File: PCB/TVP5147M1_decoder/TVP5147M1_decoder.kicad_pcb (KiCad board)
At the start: 4 copper layers, 77 parts, among them J1 Conn_02x05_Odd_Even, J2 Conn_02x05_Odd_Even, J3 Conn_02x05_Odd_Even, J4 Conn_02x01, J5 Conn_01x03_Pin, U1 AMS1117-1.8, U2 TVP5147M1IPFP, Y1 14.31818 MHz

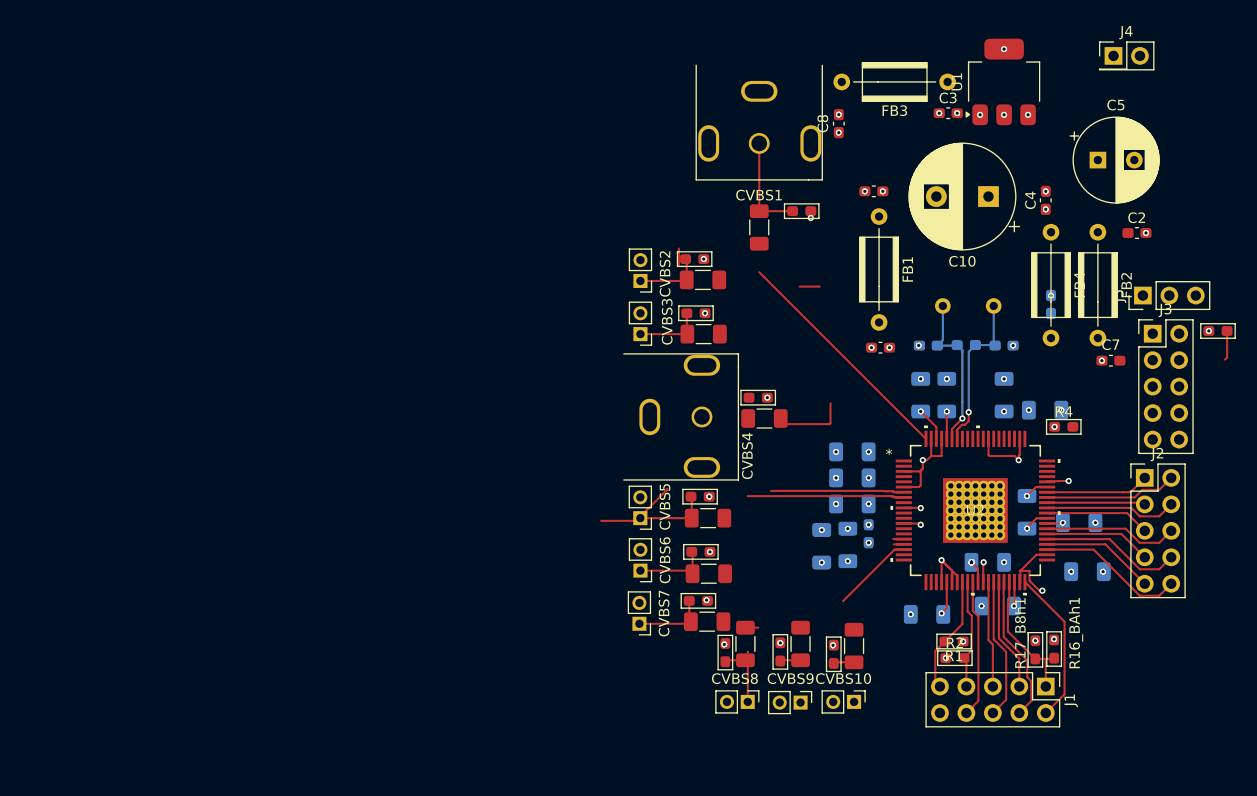
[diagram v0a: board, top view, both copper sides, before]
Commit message: decoder pcb almost done
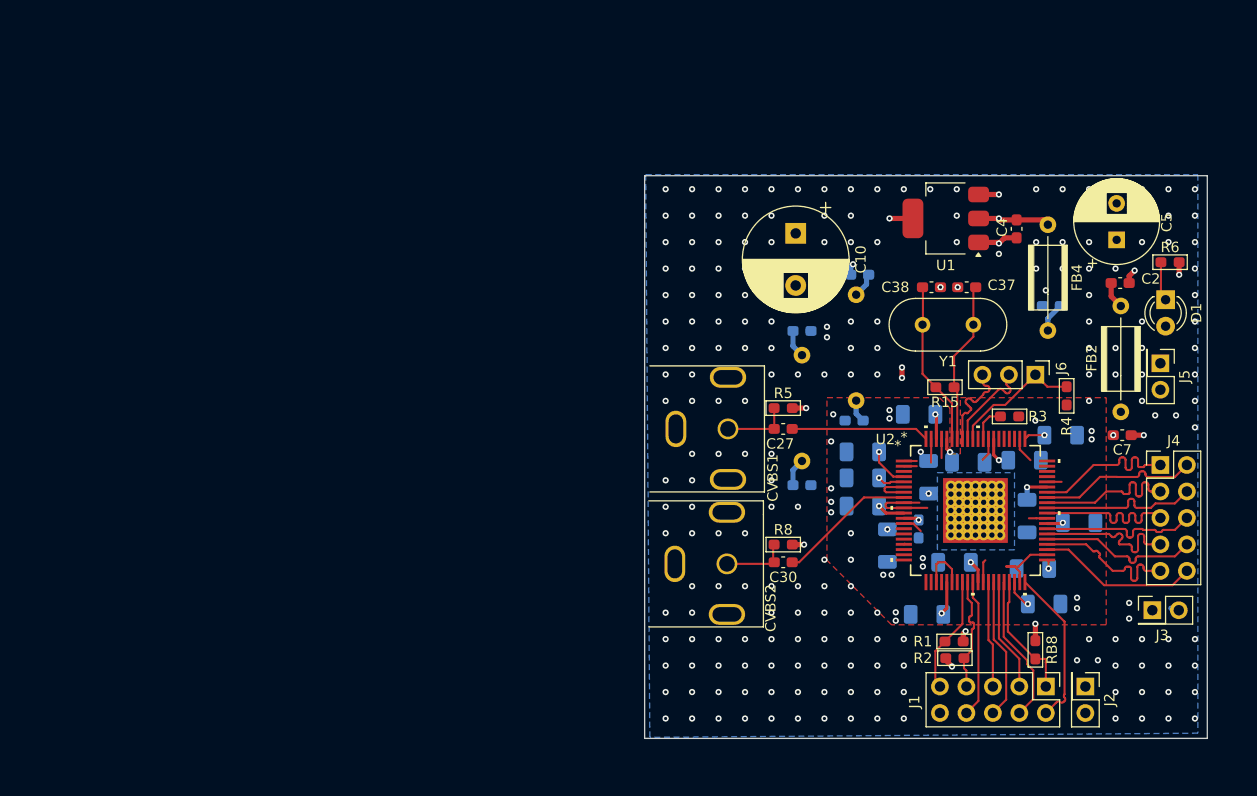
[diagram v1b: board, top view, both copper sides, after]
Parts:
- removed C28, C29, C31, C32, C33, C34, C35, C36: 0.1uF, Capacitor_SMD:C_1206_3216Metric_Pad1.33x1.80mm_HandSolder
- removed CVBS10, CVBS3, CVBS5, CVBS6, CVBS7, CVBS9: Conn_01x02, Connector_PinHeader_2.00mm:PinHeader_1x02_P2.00mm_Vertical
- removed the CVBS2 at (93.1, 69.6)
- removed CVBS8: Conn_Coaxial, Connector_PinHeader_2.00mm:PinHeader_1x02_P2.00mm_Vertical
- removed R10, R11, R12, R13, R14, R7, R9: 75Ohm, PCM_Resistor_SMD_AKL:R_0603_1608Metric_Pad1.05x0.95mm_HandSolder
- removed R16_BAh1: 10kOhm, PCM_Resistor_SMD_AKL:R_0603_1608Metric_Pad1.05x0.95mm_HandSolder
- added D1: LED_3mm, LED_THT:LED_D3.0mm, F.Cu at (143.5, 71.4)
- added J2: Conn_02x01, Connector_PinHeader_2.54mm:PinHeader_2x01_P2.54mm_Vertical, F.Cu at (135.8, 108.5)
- added NT1: NetTie_2, NetTie:NetTie-2_SMD_Pad0.5mm, F.Cu at (118.2, 78.4)
- C1, C3, C6, C8, FB1, FB3: moved to B.Cu
- C27, C30: footprint Capacitor_SMD:C_1206_3216Metric_Pad1.33x1.80mm_HandSolder -> Capacitor_SMD:C_0603_1608Metric_Pad1.08x0.95mm_HandSolder
- C37, C38, R15, Y1: moved to F.Cu
- J3: value Conn_02x05_Odd_Even -> Conn_02x01; footprint Connector_PinHeader_2.54mm:PinHeader_2x05_P2.54mm_Vertical -> Connector_PinHeader_2.54mm:PinHeader_2x01_P2.54mm_Vertical
- R6: value 75Ohm -> 5k
- moved R6 45.6 mm to (143.9, 67.8)
- moved J5 29.8 mm to (143.0, 77.5), turned to -90 degrees
- moved C8 28.5 mm to (113.6, 83.0), turned to 180 degrees
- moved J3 26.5 mm to (142.2, 101.2)
- moved FB3 22.2 mm to (113.8, 70.9), turned to -90 degrees
- moved R3 21.6 mm to (128.5, 82.6), turned to 180 degrees
- moved CVBS1 20.6 mm to (109.0, 84.0), turned to 90 degrees
- moved C27 19.5 mm to (106.8, 83.8), turned to 180 degrees
- moved R5 19.0 mm to (106.8, 81.8)
- moved C10 18.8 mm to (108.0, 65.0), turned to -90 degrees
- moved C3 17.7 mm to (114.1, 69.0), turned to 180 degrees
- moved FB1 15.2 mm to (108.6, 76.7)
- moved C6 15.2 mm to (108.6, 89.2), turned to 0 degrees
- moved C1 15.1 mm to (108.6, 74.4), turned to 0 degrees
- moved CVBS2 14.3 mm to (108.9, 96.9)
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- renumbered CVBS4 to CVBS2, J2 to J4, J4 to J5, J5 to J6, R17_B8h1 to RB8
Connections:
- C30 pad 1: CVBS_VI_2_A -> CVBS_VI_2_B
- C37 pad 2: GND -> XGND
- C38 pad 2: GND -> XGND
- J1 pad 10: unconnected-(J1-Pin_10-Pad10) -> GND
- J3 pad 1: C0 -> GND
- J3 pad 2: C1 -> GND
- R3 pad 2: C1 -> /C1
- U2 pad 1: CVBS_VI_1_B -> GND
- U2 pad 16: CVBS_VI_3_A -> GND
- U2 pad 17: CVBS_VI_3_B -> GND
- U2 pad 18: CVBS_VI_3_C -> GND
- U2 pad 2: CVBS_VI_1_C -> GND
- U2 pad 23: CVBS_VI_4_A -> GND
- U2 pad 57: C9 -> unconnected-(U2-C_9/GPIO9-Pad57)
- U2 pad 58: C8 -> unconnected-(U2-C_8/GPIO8-Pad58)
- U2 pad 59: C7 -> unconnected-(U2-C_7/GPIO7-Pad59)
- U2 pad 60: C6 -> unconnected-(U2-C_6/GPIO6-Pad60)
- U2 pad 63: C5 -> unconnected-(U2-C_5/GPIO5-Pad63)
- U2 pad 64: C4 -> unconnected-(U2-C_4/GPIO4-Pad64)
- U2 pad 65: C3 -> unconnected-(U2-C_3/GPIO3-Pad65)
- U2 pad 66: C2 -> unconnected-(U2-C_2/GPIO2-Pad66)
- U2 pad 69: C1 -> /C1
- U2 pad 7: CVBS_VI_2_A -> GND
- U2 pad 70: C0 -> unconnected-(U2-C_0/GPIO0-Pad70)
- U2 pad 9: CVBS_VI_2_C -> GND
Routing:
- net CVBS_VI_2_A: track 19.2 -> 0.00 mm
- net Net-(CVBS5-Pin_1): track 14.8 -> 0.00 mm
- net FID: track 0.00 -> 12.8 mm
- net GND: track 43.1 -> 54.1 mm, vias 48 -> 231
- net +1.8V: track 0.00 -> 11.1 mm, vias 4 -> 2
- net CVBS_VI_1_A: track 24.3 -> 13.2 mm
- net A3.3VDD: track 0.00 -> 9.27 mm, vias 3 -> 2
- net HS/CS: track 0.00 -> 9.26 mm
- net VS/VBLK: track 0.00 -> 9.25 mm
- net CVBS_VI_3_C: track 7.89 -> 0.00 mm
- net D1.8VDD: track 4.44 -> 12.3 mm, vias 7 -> 4
- net Net-(CVBS7-Pin_1): track 7.36 -> 0.00 mm
- net Net-(CVBS6-Pin_1): track 7.26 -> 0.00 mm
- net +3.3V: track 0.00 -> 7.21 mm, vias 2 -> 1
- net Net-(CVBS8-Pin_1): track 7.11 -> 0.00 mm
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- added copper zone on B.Cu, net GND
- added copper zone on F.Cu, net GND
- added copper zone on In1.Cu, net XGND
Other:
- board outline added: 54 x 54 mm

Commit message: added basic hash_drbg
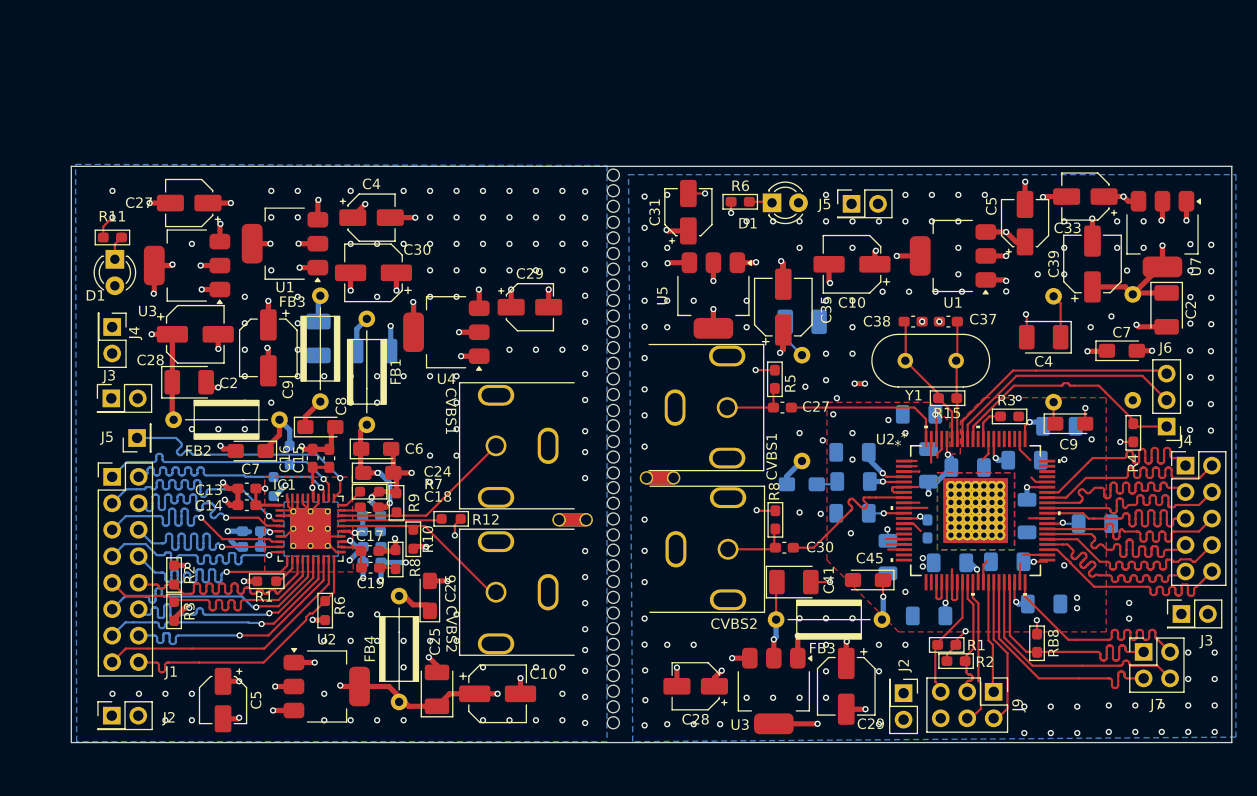
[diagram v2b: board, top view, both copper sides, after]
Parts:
- removed the FB3 at (113.8, 70.9)
- added C1: 33uF, Capacitor_Tantalum_SMD:CP_EIA-3528-15_AVX-H_Pad1.50x2.35mm_HandSolder, B.Cu at (67.4, 76.3)
- added C10: 22uF, Capacitor_SMD:CP_Elec_5x5.7, F.Cu at (79.4, 109.2)
- added C11: 0.01uF, Capacitor_SMD:C_0603_1608Metric_Pad1.08x0.95mm_HandSolder, B.Cu at (55.8, 95.1)
- added C12: 0.1uF, Capacitor_SMD:C_0603_1608Metric_Pad1.08x0.95mm_HandSolder, B.Cu at (55.8, 93.6)
- added C13: 0.01uF, Capacitor_SMD:C_0603_1608Metric_Pad1.08x0.95mm_HandSolder, F.Cu at (55.3, 89.5)
- added C14: 0.1uF, Capacitor_SMD:C_0603_1608Metric_Pad1.08x0.95mm_HandSolder, F.Cu at (55.3, 91.1)
- added C15: 0.01uF, Capacitor_SMD:C_0603_1608Metric_Pad1.08x0.95mm_HandSolder, F.Cu at (63.2, 86.6)
- added C16: 0.1uF, Capacitor_SMD:C_0603_1608Metric_Pad1.08x0.95mm_HandSolder, F.Cu at (61.6, 86.6)
- added C17: 12nF, Capacitor_SMD:C_0603_1608Metric_Pad1.08x0.95mm_HandSolder, F.Cu at (67.1, 95.5)
- added C18: 2.2nF, Capacitor_SMD:C_0603_1608Metric_Pad1.08x0.95mm_HandSolder, F.Cu at (67.1, 91.3)
- added C19: 150nF, Capacitor_SMD:C_0603_1608Metric_Pad1.08x0.95mm_HandSolder, F.Cu at (67.2, 97.1)
- added C2: 33uF, Capacitor_Tantalum_SMD:CP_EIA-3528-15_AVX-H_Pad1.50x2.35mm_HandSolder, F.Cu at (49.8, 79.3)
- added C20: 0.01uF, Capacitor_SMD:C_0603_1608Metric_Pad1.08x0.95mm_HandSolder, B.Cu at (67.3, 95.1)
- added C21: 0.1uF, Capacitor_SMD:C_0603_1608Metric_Pad1.08x0.95mm_HandSolder, B.Cu at (67.3, 96.6)
- added C22: 0.01uF, Capacitor_SMD:C_0603_1608Metric_Pad1.08x0.95mm_HandSolder, B.Cu at (67.3, 92.1)
- added C23: 0.1uF, Capacitor_SMD:C_0603_1608Metric_Pad1.08x0.95mm_HandSolder, B.Cu at (67.3, 93.6)
- added C24: 1uF, Capacitor_Tantalum_SMD:CP_EIA-3216-18_Kemet-A_Pad1.58x1.35mm_HandSolder, F.Cu at (67.9, 88.0)
- added C25: 33uF, Capacitor_Tantalum_SMD:CP_EIA-3528-15_AVX-H_Pad1.50x2.35mm_HandSolder, F.Cu at (73.6, 108.8)
- added C26: 10uF, Capacitor_Tantalum_SMD:CP_EIA-3216-18_Kemet-A_Pad1.58x1.35mm_HandSolder, F.Cu at (72.9, 99.8)
- added C27: 10uF, Capacitor_SMD:CP_Elec_4x5.7, F.Cu at (49.8, 62.1)
- added C28: 22uF, Capacitor_SMD:CP_Elec_5x5.7, F.Cu at (50.4, 74.7)
- added C28: 10uF, Capacitor_SMD:CP_Elec_4x5.7, F.Cu at (98.4, 108.5)
- added C29: 10uF, Capacitor_SMD:CP_Elec_4x5.7, F.Cu at (82.5, 72.1)
- added C29: 22uF, Capacitor_SMD:CP_Elec_5x5.7, F.Cu at (112.8, 108.5)
- added C30: 22uF, Capacitor_SMD:CP_Elec_5x5.7, F.Cu at (67.5, 68.8)
- added C31: 10uF, Capacitor_SMD:CP_Elec_4x5.7, F.Cu at (97.7, 63.0)
- added C33: 10uF, Capacitor_SMD:CP_Elec_4x5.7, F.Cu at (135.8, 61.5)
- added C35: 22uF, Capacitor_SMD:CP_Elec_5x5.7, F.Cu at (106.8, 72.1)
- added C39: 22uF, Capacitor_SMD:CP_Elec_5x5.7, F.Cu at (136.5, 68.0)
- added C4: 10uF, Capacitor_SMD:CP_Elec_4x5.7, F.Cu at (67.3, 63.5)
- added C41: 33uF, Capacitor_Tantalum_SMD:CP_EIA-3528-15_AVX-H_Pad1.50x2.35mm_HandSolder, F.Cu at (107.8, 98.5)
- added C45: 10uF, Capacitor_Tantalum_SMD:CP_EIA-3216-18_Kemet-A_Pad1.58x1.35mm_HandSolder, F.Cu at (114.9, 98.3)
- added C5: 10uF, Capacitor_SMD:CP_Elec_4x5.7, F.Cu at (53.0, 109.8)
- added C6: 10uF, Capacitor_Tantalum_SMD:CP_EIA-3216-18_Kemet-A_Pad1.58x1.35mm_HandSolder, F.Cu at (67.7, 85.7)
- added C7: 10uF, Capacitor_Tantalum_SMD:CP_EIA-3216-18_Kemet-A_Pad1.58x1.35mm_HandSolder, F.Cu at (55.7, 85.9)
- added C9: 22uF, Capacitor_SMD:CP_Elec_5x5.7, F.Cu at (57.4, 76.0)
- added CVBS1: Conn_Coaxial, LocalLibrary:CC-132-B1, F.Cu at (71.7, 85.3)
- added CVBS2: Conn_Coaxial, LocalLibrary:CC-132-B1, F.Cu at (71.7, 99.3)
- added D1: LED_3mm, LED_THT:LED_D3.0mm, F.Cu at (42.7, 67.5)
- added FB1: Ferrite_Bead, PCM_Ferrite_THT_AKL:Ferrite_L6.0mm_D3.5mm_P10.16mm, F.Cu at (66.8, 73.2)
- added FB2: Ferrite_Bead, PCM_Ferrite_THT_AKL:Ferrite_L6.0mm_D3.5mm_P10.16mm, F.Cu at (48.3, 82.9)
- added FB3: Ferrite_Bead, PCM_Ferrite_THT_AKL:Ferrite_L6.0mm_D3.5mm_P10.16mm, F.Cu at (106.1, 102.1)
- added FB3: Ferrite_Bead, PCM_Ferrite_THT_AKL:Ferrite_L6.0mm_D3.5mm_P10.16mm, F.Cu at (62.4, 71.0)
- added FB4: Ferrite_Bead, PCM_Ferrite_THT_AKL:Ferrite_L6.0mm_D3.5mm_P10.16mm, F.Cu at (69.9, 110.0)
- added IC1: ADV7393BCPZ-REEL, Package_CSP:LFCSP-40-1EP_6x6mm_P0.5mm_EP3.9x3.9mm_ThermalVias, F.Cu at (61.4, 93.4)
- added J2: Conn_02x01, Connector_PinHeader_2.54mm:PinHeader_2x01_P2.54mm_Vertical, F.Cu at (42.4, 111.3)
- added J3: Conn_02x01, Connector_PinHeader_2.54mm:PinHeader_2x01_P2.54mm_Vertical, F.Cu at (42.3, 80.9)
- added J4: Conn_02x01, Connector_PinHeader_2.54mm:PinHeader_2x01_P2.54mm_Vertical, F.Cu at (42.4, 74.0)
- added J5: Conn_01x01, Connector_PinHeader_2.54mm:PinHeader_1x01_P2.54mm_Vertical, F.Cu at (44.8, 84.7)
- added J7: Conn_02x02_Odd_Even, Connector_PinHeader_2.54mm:PinHeader_2x02_P2.54mm_Vertical, F.Cu at (141.4, 105.2)
- added J9: Conn_02x03_Odd_Even, Connector_PinHeader_2.54mm:PinHeader_2x03_P2.54mm_Vertical, F.Cu at (127.0, 109.0)
- added NT1: NetTie_2, NetTie:NetTie-2_THT_Pad1.0mm, F.Cu at (87.9, 92.5)
- added NT3: NetTie_2, NetTie:NetTie-2_THT_Pad1.0mm, F.Cu at (96.3, 88.5)
- added R1: 5k, PCM_Resistor_SMD_AKL:R_0603_1608Metric_Pad0.98x0.95mm_HandSolder, F.Cu at (57.2, 98.4)
- added R10: 75, PCM_Resistor_SMD_AKL:R_0603_1608Metric_Pad0.98x0.95mm_HandSolder, F.Cu at (71.3, 94.4)
- added R11: 5k, PCM_Resistor_SMD_AKL:R_0603_1608Metric_Pad1.05x0.95mm_HandSolder, F.Cu at (42.4, 65.4)
- added R12: 0, PCM_Resistor_SMD_AKL:R_0603_1608Metric_Pad0.98x0.95mm_HandSolder, F.Cu at (74.9, 92.4)
- added R2: 2k2, PCM_Resistor_SMD_AKL:R_0603_1608Metric_Pad0.98x0.95mm_HandSolder, F.Cu at (48.3, 97.8)
- added R3: 2k2, PCM_Resistor_SMD_AKL:R_0603_1608Metric_Pad0.98x0.95mm_HandSolder, F.Cu at (48.3, 101.3)
- added R4: 4k7, PCM_Resistor_SMD_AKL:R_0603_1608Metric_Pad0.98x0.95mm_HandSolder, B.Cu at (57.9, 89.3)
- added R5: 4k7, PCM_Resistor_SMD_AKL:R_0603_1608Metric_Pad0.98x0.95mm_HandSolder, B.Cu at (59.4, 86.3)
- added R6: 4k7, PCM_Resistor_SMD_AKL:R_0603_1608Metric_Pad0.98x0.95mm_HandSolder, F.Cu at (62.8, 101.2)
- added R7: 510, PCM_Resistor_SMD_AKL:R_0603_1608Metric_Pad0.98x0.95mm_HandSolder, F.Cu at (67.1, 89.8)
- added R8: 170, PCM_Resistor_SMD_AKL:R_0603_1608Metric_Pad0.98x0.95mm_HandSolder, F.Cu at (69.6, 96.3)
- added R9: 75, PCM_Resistor_SMD_AKL:R_0603_1608Metric_Pad0.98x0.95mm_HandSolder, F.Cu at (69.7, 90.9)
- added REF**: ToolingHole_1.152mm, MountingHole:ToolingHole_1.152mm, F.Cu at (90.5, 110.5)
- added REF**: ToolingHole_1.152mm, MountingHole:ToolingHole_1.152mm, F.Cu at (90.5, 109.0)
- added REF**: ToolingHole_1.152mm, MountingHole:ToolingHole_1.152mm, F.Cu at (90.5, 89.4)
- added REF**: ToolingHole_1.152mm, MountingHole:ToolingHole_1.152mm, F.Cu at (90.5, 68.5)
- added REF**: ToolingHole_1.152mm, MountingHole:ToolingHole_1.152mm, F.Cu at (90.5, 83.5)
- added REF**: ToolingHole_1.152mm, MountingHole:ToolingHole_1.152mm, F.Cu at (90.5, 90.9)
- added REF**: ToolingHole_1.152mm, MountingHole:ToolingHole_1.152mm, F.Cu at (90.5, 96.9)
- added REF**: ToolingHole_1.152mm, MountingHole:ToolingHole_1.152mm, F.Cu at (90.5, 107.5)
- added REF**: ToolingHole_1.152mm, MountingHole:ToolingHole_1.152mm, F.Cu at (90.5, 77.5)
- added REF**: ToolingHole_1.152mm, MountingHole:ToolingHole_1.152mm, F.Cu at (90.5, 67.0)
- added REF**: ToolingHole_1.152mm, MountingHole:ToolingHole_1.152mm, F.Cu at (90.5, 104.5)
- added REF**: ToolingHole_1.152mm, MountingHole:ToolingHole_1.152mm, F.Cu at (90.5, 88.0)
- added REF**: ToolingHole_1.152mm, MountingHole:ToolingHole_1.152mm, F.Cu at (90.5, 62.4)
- added REF**: ToolingHole_1.152mm, MountingHole:ToolingHole_1.152mm, F.Cu at (90.5, 106.0)
- added REF**: ToolingHole_1.152mm, MountingHole:ToolingHole_1.152mm, F.Cu at (90.5, 112.0)
- added REF**: ToolingHole_1.152mm, MountingHole:ToolingHole_1.152mm, F.Cu at (90.5, 100.0)
- added REF**: ToolingHole_1.152mm, MountingHole:ToolingHole_1.152mm, F.Cu at (90.5, 74.5)
- added REF**: ToolingHole_1.152mm, MountingHole:ToolingHole_1.152mm, F.Cu at (90.5, 98.4)
- added REF**: ToolingHole_1.152mm, MountingHole:ToolingHole_1.152mm, F.Cu at (90.5, 60.9)
- added REF**: ToolingHole_1.152mm, MountingHole:ToolingHole_1.152mm, F.Cu at (90.5, 86.5)
- added REF**: ToolingHole_1.152mm, MountingHole:ToolingHole_1.152mm, F.Cu at (90.5, 101.5)
- added REF**: ToolingHole_1.152mm, MountingHole:ToolingHole_1.152mm, F.Cu at (90.5, 94.0)
- added REF**: ToolingHole_1.152mm, MountingHole:ToolingHole_1.152mm, F.Cu at (90.5, 80.5)
- added REF**: ToolingHole_1.152mm, MountingHole:ToolingHole_1.152mm, F.Cu at (90.5, 59.4)
- added REF**: ToolingHole_1.152mm, MountingHole:ToolingHole_1.152mm, F.Cu at (90.5, 65.5)
- added REF**: ToolingHole_1.152mm, MountingHole:ToolingHole_1.152mm, F.Cu at (90.5, 85.0)
- added REF**: ToolingHole_1.152mm, MountingHole:ToolingHole_1.152mm, F.Cu at (90.5, 70.0)
- added REF**: ToolingHole_1.152mm, MountingHole:ToolingHole_1.152mm, F.Cu at (90.5, 71.5)
- added REF**: ToolingHole_1.152mm, MountingHole:ToolingHole_1.152mm, F.Cu at (90.5, 82.0)
- added REF**: ToolingHole_1.152mm, MountingHole:ToolingHole_1.152mm, F.Cu at (90.5, 64.0)
- added REF**: ToolingHole_1.152mm, MountingHole:ToolingHole_1.152mm, F.Cu at (90.5, 95.4)
- added REF**: ToolingHole_1.152mm, MountingHole:ToolingHole_1.152mm, F.Cu at (90.5, 92.4)
- added REF**: ToolingHole_1.152mm, MountingHole:ToolingHole_1.152mm, F.Cu at (90.5, 76.0)
- added REF**: ToolingHole_1.152mm, MountingHole:ToolingHole_1.152mm, F.Cu at (90.5, 79.0)
- added REF**: ToolingHole_1.152mm, MountingHole:ToolingHole_1.152mm, F.Cu at (90.5, 103.0)
- added REF**: ToolingHole_1.152mm, MountingHole:ToolingHole_1.152mm, F.Cu at (90.5, 73.0)
- added U1: AMS1117-1.8, Package_TO_SOT_SMD:SOT-223-3_TabPin2, F.Cu at (59.0, 66.0)
- added U2: AMS1117-1.8, Package_TO_SOT_SMD:SOT-223-3_TabPin2, F.Cu at (63.0, 108.5)
- added U3: AMS1117-1.8, Package_TO_SOT_SMD:SOT-223-3_TabPin2, F.Cu at (105.9, 109.0)
- added U3: AMS1117-3.3, Package_TO_SOT_SMD:SOT-223-3_TabPin2, F.Cu at (49.6, 68.1)
- added U4: AMS1117-3.3, Package_TO_SOT_SMD:SOT-223-3_TabPin2, F.Cu at (74.5, 74.5)
- added U5: AMS1117-3.3, Package_TO_SOT_SMD:SOT-223-3_TabPin2, F.Cu at (100.1, 71.0)
- added U7: AMS1117-3.3, Package_TO_SOT_SMD:SOT-223-3_TabPin2, F.Cu at (143.2, 65.1)
- C1, C2, C3, C4: footprint Capacitor_SMD:C_0603_1608Metric_Pad1.08x0.95mm_HandSolder -> Capacitor_Tantalum_SMD:CP_EIA-3528-15_AVX-H_Pad1.50x2.35mm_HandSolder
- C10: footprint Capacitor_THT:CP_Radial_D10.0mm_P5.00mm -> Capacitor_SMD:CP_Elec_5x5.7
- C5: footprint Capacitor_THT:CP_Radial_D8.0mm_P3.50mm -> Capacitor_SMD:CP_Elec_4x5.7
- C6, C7: footprint Capacitor_SMD:C_0603_1608Metric_Pad1.08x0.95mm_HandSolder -> Capacitor_Tantalum_SMD:CP_EIA-3216-18_Kemet-A_Pad1.58x1.35mm_HandSolder
- C8, C9: footprint Capacitor_SMD:C_0603_1608Metric_Pad1.08x0.95mm_HandSolder -> Capacitor_Tantalum_SMD:CP_EIA-3216-18_Kemet-A_Pad1.58x1.35mm_HandSolder; moved to F.Cu
- FB2, FB4: moved to B.Cu
- J1: value Conn_02x05_Odd_Even -> Conn_02x08_Odd_Even; footprint Connector_PinHeader_2.54mm:PinHeader_2x05_P2.54mm_Vertical -> Connector_PinHeader_2.54mm:PinHeader_2x08_P2.54mm_Vertical
- moved J1 91.8 mm to (42.4, 88.4), turned to 0 degrees
- moved C3 52.3 mm to (62.2, 75.1), turned to -90 degrees
- moved C8 51.2 mm to (62.4, 83.6), turned to 0 degrees
- moved R6 41.7 mm to (102.7, 62.0), turned to 180 degrees
- moved D1 38.9 mm to (105.7, 62.1), turned to 0 degrees
- moved J5 33.4 mm to (113.4, 62.2), turned to 0 degrees
- moved J2 17.5 mm to (118.3, 109.2)
- moved J6 13.5 mm to (143.6, 83.6), turned to 180 degrees
- moved C9 11.4 mm to (134.3, 83.3), turned to 0 degrees
- moved C4 10.7 mm to (131.8, 75.0), turned to 180 degrees
- moved C5 8.93 mm to (130.0, 64.0)
- moved C7 8.10 mm to (139.3, 76.3)
- moved R4 7.32 mm to (140.4, 84.2)
- moved FB4 6.89 mm to (132.8, 71.1)
- moved C10 6.16 mm to (113.4, 68.0), turned to 180 degrees
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- renumbered NT1 to NT2
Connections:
- net +1.8V renamed +1.8VPD
- C1 pad 1: +3.3V -> +3.3VPA
- C2 pad 1: +3.3V -> +3.3VPD
- C5 pad 1: +3.3V -> +5V
- C8 pad 1: A1.8VDD -> D1.8VDD
- CVBS1 pad 2: GND -> CGND
- CVBS2 pad 2: GND -> CGND
- D1 pad 2: +3.3V -> +5V
- FB1 pad 1: +3.3V -> +3.3VPA
- FB2 pad 1: +3.3V -> +3.3VPD
- J1 pad 1: GLCO/I2CA -> ~{VSYNC}
- J1 pad 10: GND -> SCL
- J1 pad 2: DATACLK -> ~{HSYNC}
- J1 pad 3: FSS -> YE0
- J1 pad 4: AVID -> YE1
- J1 pad 5: PWDN -> YE2
- J1 pad 6: RESETB -> YE3
- J1 pad 7: SDA -> YE4
- J1 pad 8: INTREQ -> YE5
- J1 pad 9: SCL -> SDA
- J5 pad 1: +3.3V -> +5V
- R5 pad 2: GND -> CGND
- R8 pad 2: GND -> CGND
- U1 pad 3: +3.3V -> +5V
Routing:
- net GND: track 54.1 -> 167.9 mm, vias 231 -> 308
- net +3.3VPD: track 0.00 -> 36.3 mm, vias 0 -> 6
- net +1.8VPA: track 0.00 -> 32.3 mm, vias 0 -> 6
- net +5V: track 0.00 -> 30.6 mm, vias 0 -> 14
- net SDA: track 11.2 -> 37.5 mm
- net Net-(IC1-~{RESET}): track 0.00 -> 26.3 mm
- net Net-(IC1-CLKIN): track 0.00 -> 26.3 mm
- net SCL: track 11.3 -> 37.4 mm
- net YE8: track 0.00 -> 24.7 mm, vias 0 -> 1
- net Net-(IC1-SFL): track 0.00 -> 24.7 mm, vias 0 -> 1
- net ~{VSYNC}: track 0.00 -> 24.7 mm, vias 0 -> 1
- net YE6: track 0.00 -> 24.7 mm, vias 0 -> 1
- net YE9: track 0.00 -> 24.7 mm, vias 0 -> 1
- net YE7: track 0.00 -> 24.7 mm, vias 0 -> 1
- net YE2: track 0.00 -> 24.6 mm, vias 0 -> 1
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- added copper zone on In2.Cu, net +1.8VPA
- added copper zone on In2.Cu, net +3.3VPA
- added copper zone on In2.Cu, net +3.3VPD
- added copper zone on In2.Cu, net +5V
- added copper zone on In1.Cu, net CGND
- removed copper zone on In2.Cu, net +3.3V
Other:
- board size 54 x 54 mm -> 111.4 x 55.3 mm

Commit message: hash_drbg is working, trying to add double_hash_drbg
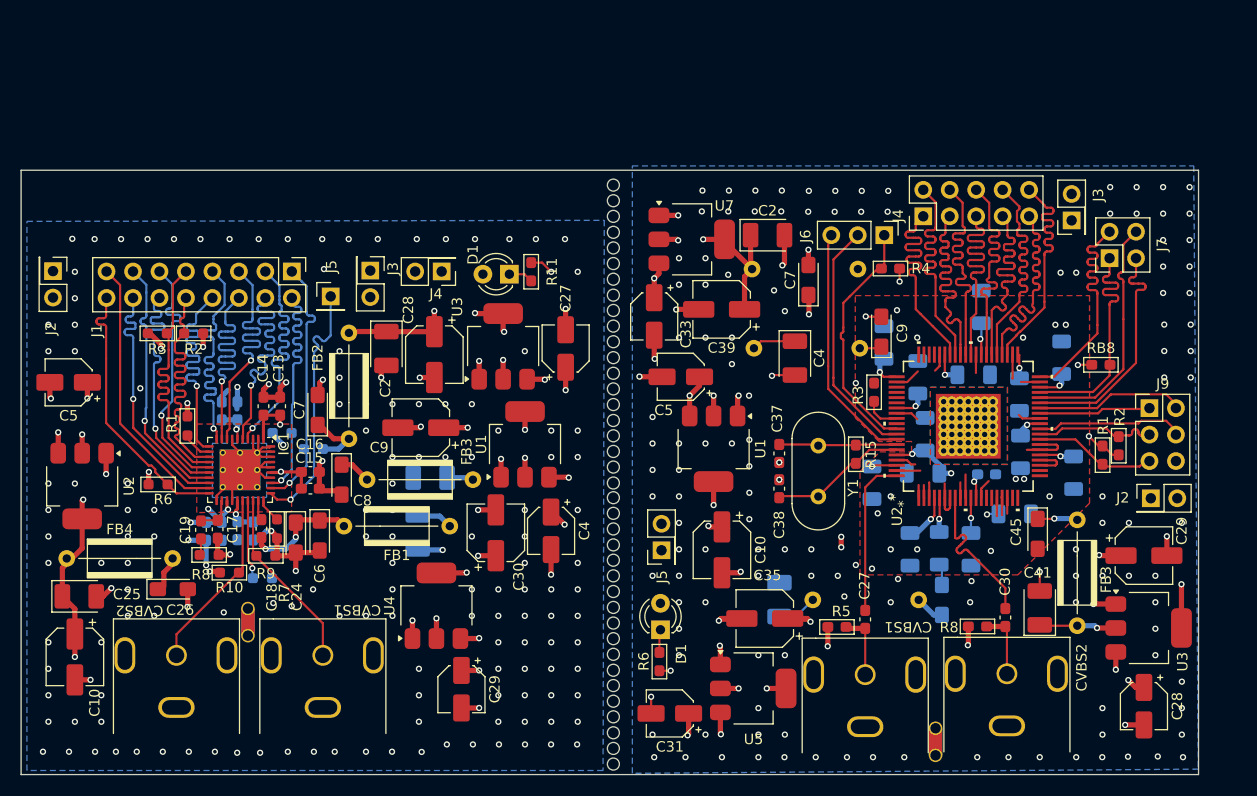
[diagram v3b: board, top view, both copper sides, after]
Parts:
- added REF**: ToolingHole_1.152mm, MountingHole:ToolingHole_1.152mm, F.Cu at (90.5, 114.5)
- added REF**: ToolingHole_1.152mm, MountingHole:ToolingHole_1.152mm, F.Cu at (90.5, 116.0)
- R12: moved to B.Cu
- moved C31 48.1 mm to (95.9, 111.1), turned to 180 degrees
- moved U7 45.2 mm to (98.0, 65.6), turned to 0 degrees
- moved R6 44.8 mm to (94.9, 106.1), turned to -90 degrees
- moved C28 43.1 mm to (141.4, 110.4), turned to -90 degrees
- moved J2 43.0 mm to (36.7, 68.7), turned to -90 degrees
- moved C33 42.9 mm to (94.4, 73.0), turned to -90 degrees
- moved D1 42.4 mm to (95.0, 103.1), turned to 90 degrees
- moved C10 40.7 mm to (38.8, 105.7), turned to -90 degrees
- moved R11 40.3 mm to (82.6, 68.7), turned to 90 degrees
- moved J3 39.2 mm to (134.5, 63.8), turned to 90 degrees
- moved C2 39.0 mm to (105.3, 65.2), turned to 0 degrees
- moved C27 38.7 mm to (85.9, 76.1), turned to 90 degrees
- moved J7 37.9 mm to (138.1, 67.4), turned to 90 degrees
- moved J5 37.9 mm to (95.1, 95.4), turned to 90 degrees
- moved U5 37.9 mm to (103.9, 108.7), turned to 0 degrees
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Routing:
- net Net-(IC1-DAC_2): track 9.74 -> 7.65 mm, vias 0 -> 1
- net Net-(CVBS1-In): track 6.23 -> 8.12 mm
- net GND: track 167.9 -> 166.1 mm, vias 308 -> 330
- net Net-(CVBS2-In): track 6.20 -> 8.00 mm
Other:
- board size 111.4 x 55.3 mm -> 113 x 58 mm
